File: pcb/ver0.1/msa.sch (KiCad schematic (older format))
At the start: 55 parts, among them J1 USB_A, J2 SWD Prog, U1 MCP1702, U2 MP23DB01HPTR, U3 W25Q128JV, U4 RP2040, U5 MP23DB01HPTR, U6 MP23DB01HPTR, U7 MP23DB01HPTR, Y1 H130B-12.000-20-3050-EXT-TR

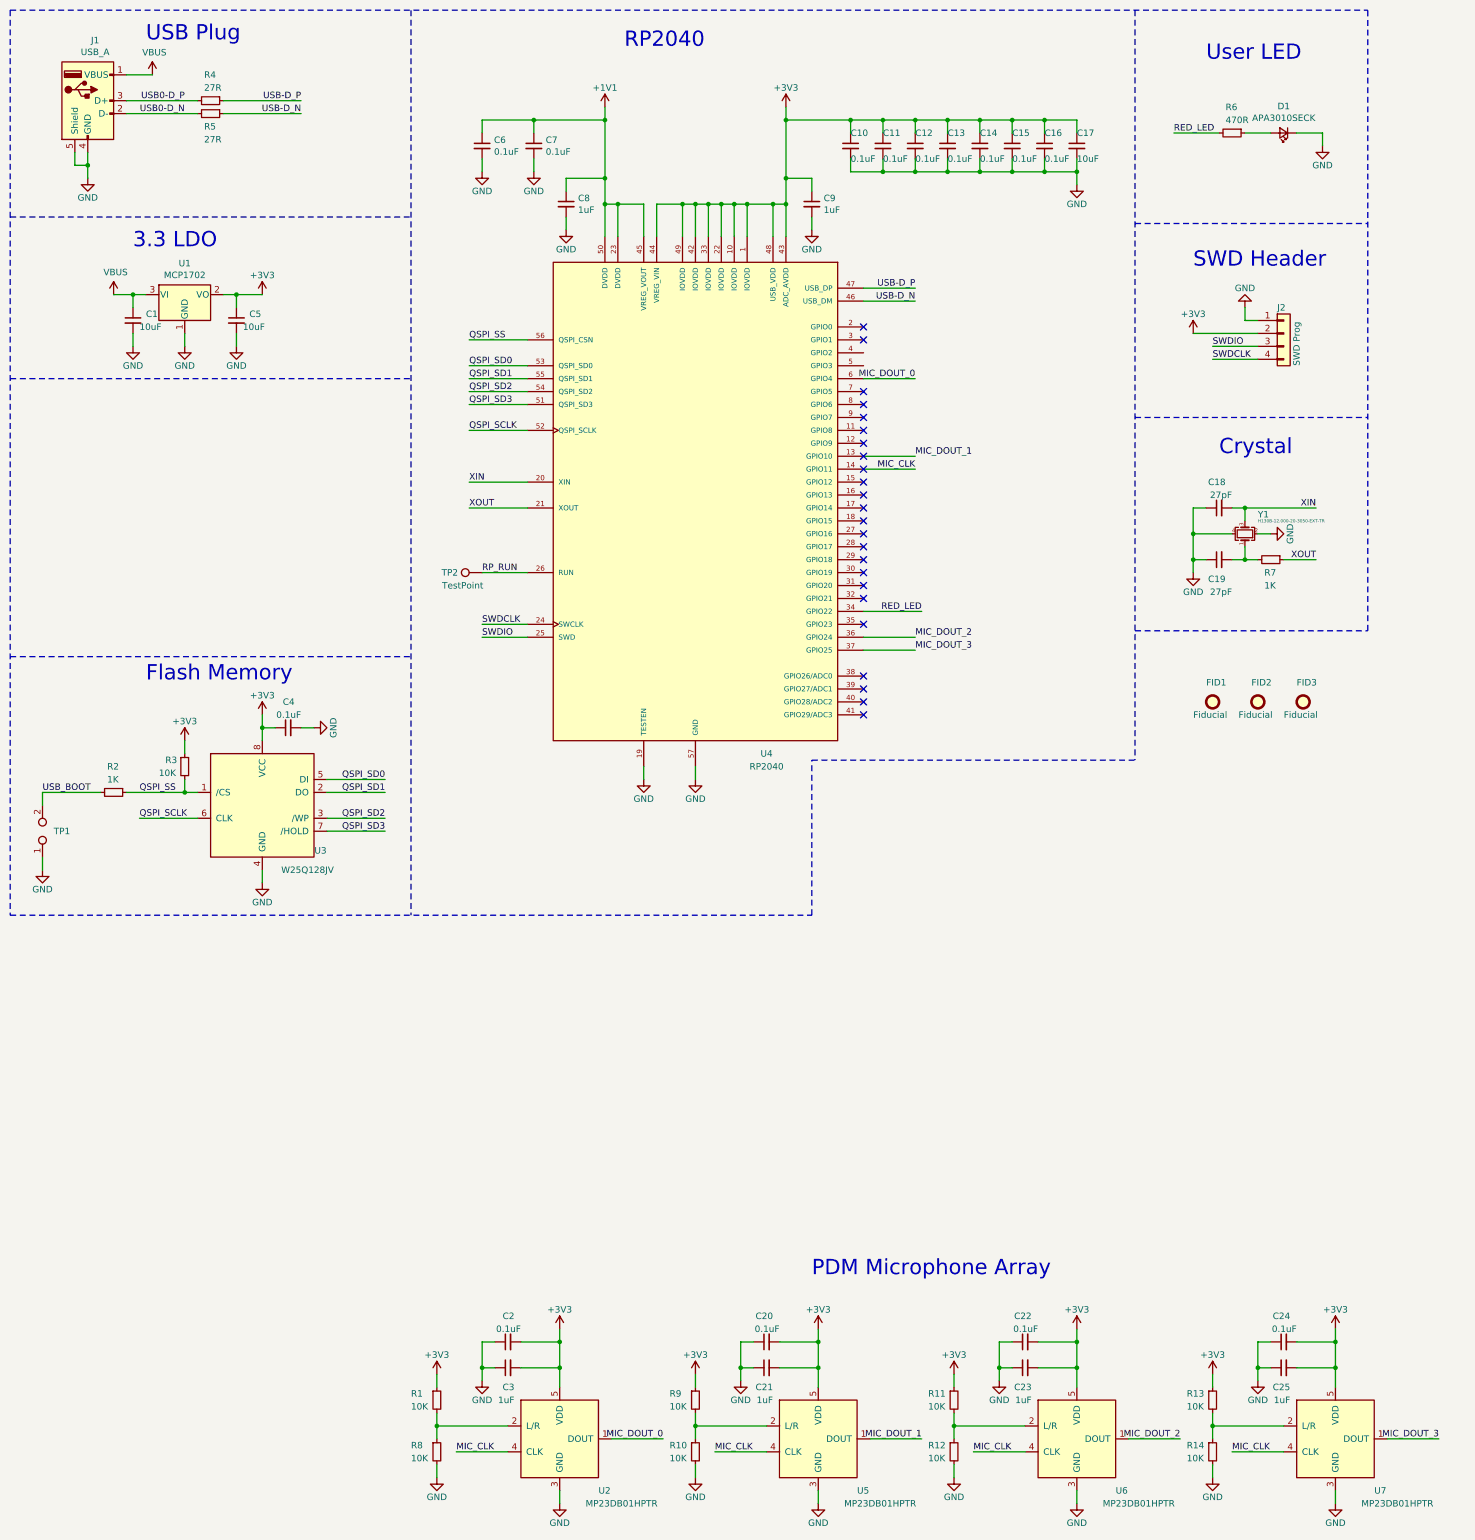
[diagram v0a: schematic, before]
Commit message: add test pads, last check before order PCB
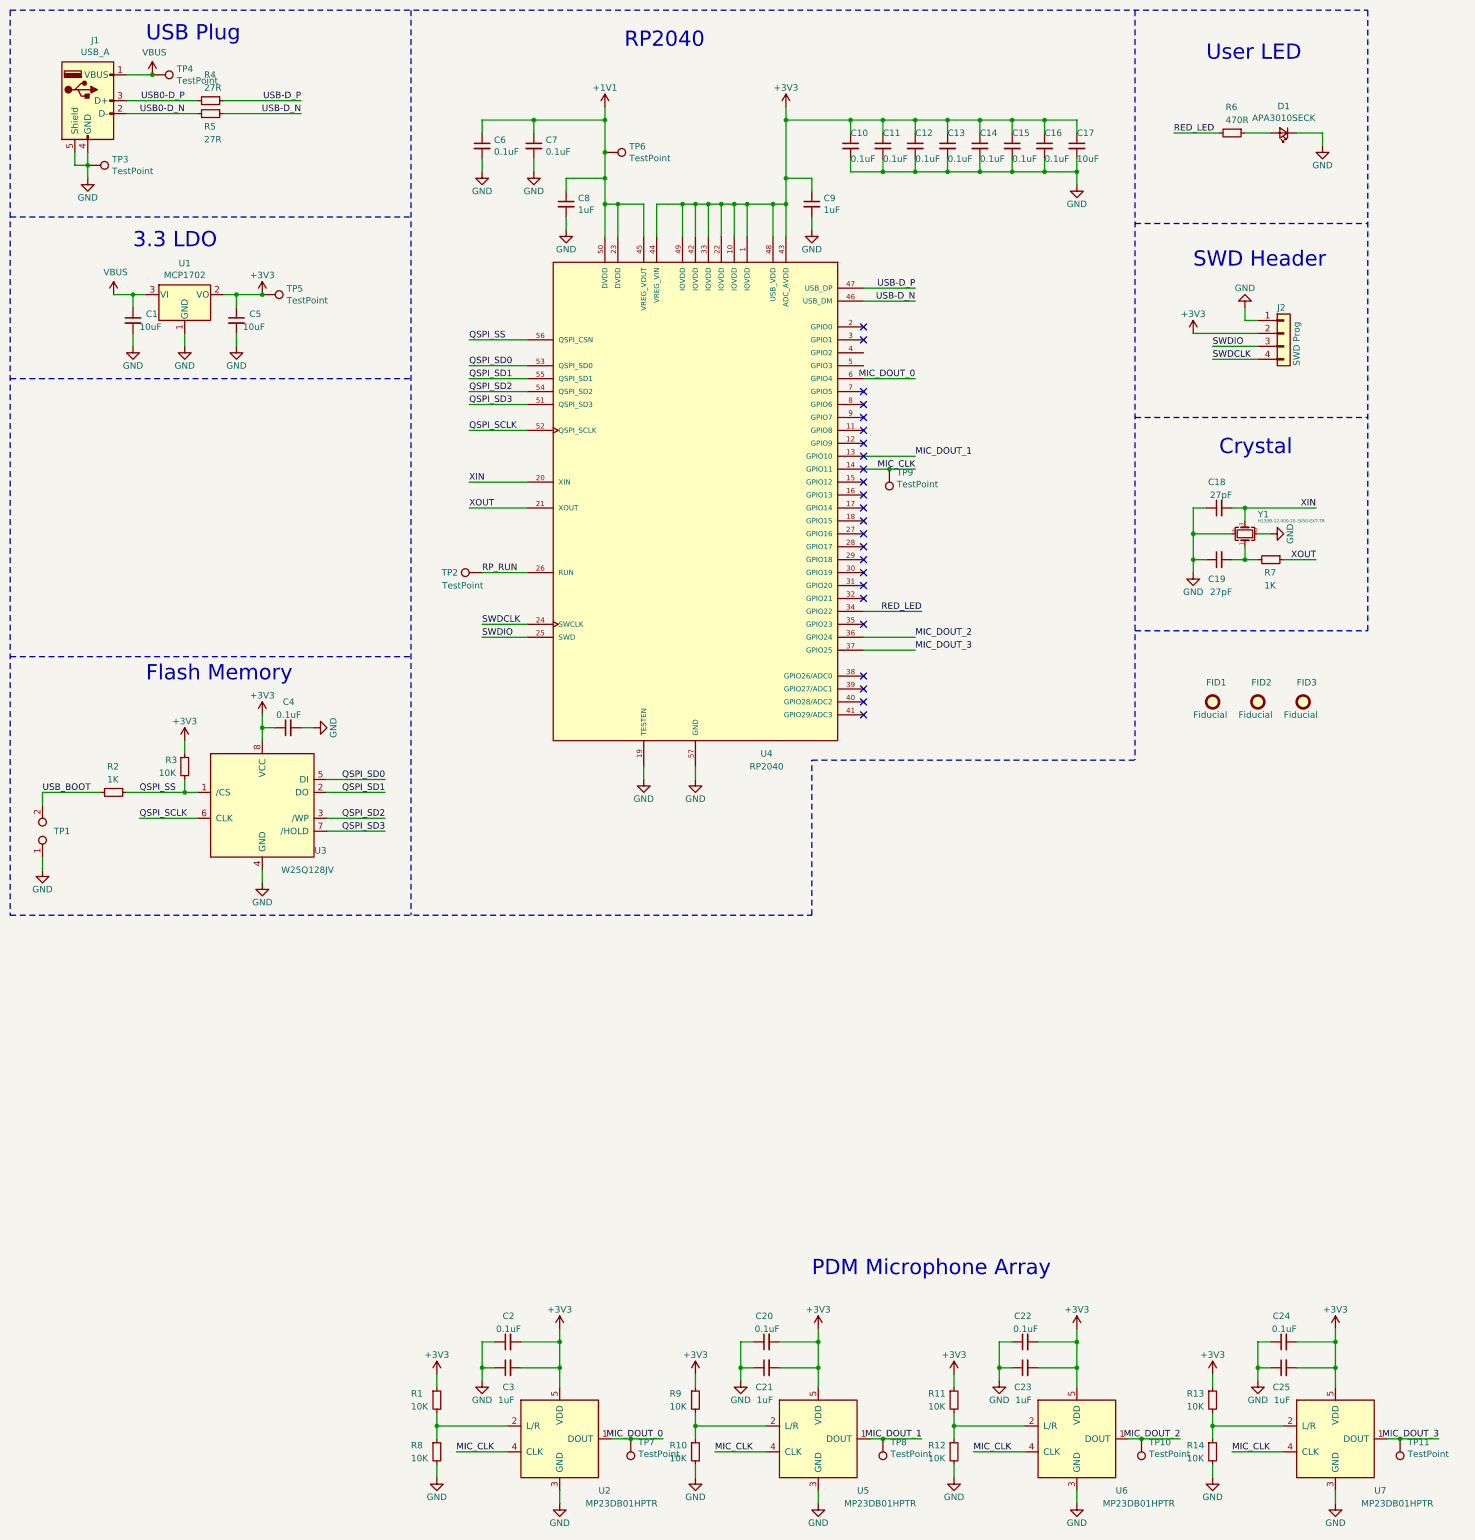
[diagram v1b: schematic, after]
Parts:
- added TP10, TP11, TP3, TP4, TP5, TP6, TP7, TP8, TP9: TestPoint, mico:SMD_1x01_P1.27mm, symbol Connector:TestPoint
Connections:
- net +1V1: now also TP6.1
- net +3V3: now also TP5.1
- net GND: now also TP3.1
- net MIC_CLK: now also TP9.1
- net MIC_DOUT_0: now also TP7.1
- net MIC_DOUT_1: now also TP8.1
- net MIC_DOUT_2: now also TP10.1
- net MIC_DOUT_3: now also TP11.1
- net VBUS: now also TP4.1
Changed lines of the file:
@@
 	4650 1450 4250 1450
 Wire Wire Line
-	5200 1450 5200 1900
+	5200 1450 5200 1700
 Wire Wire Line
 	4650 1450 5200 1450
@@
 	1100 1700 1100 1800
 Wire Wire Line
-	1100 1800 1200 1800
-Wire Wire Line
 	1200 1800 1200 1700
 Wire Wire Line
@@
 $EndComp
 Wire Wire Line
-	5250 11650 5650 11650
+	5250 11650 5400 11650
 Wire Wire Line
 	4450 11750 4050 11750
@@
 $EndComp
 Wire Wire Line
-	7250 11650 7650 11650
+	7250 11650 7350 11650
 Wire Wire Line
 	6450 11750 6050 11750
@@
 $EndComp
 Wire Wire Line
-	9250 11650 9650 11650
+	9250 11650 9350 11650
 Wire Wire Line
 	8450 11750 8050 11750
@@
 $EndComp
 Wire Wire Line
-	11250 11650 11650 11650
+	11250 11650 11350 11650
 Wire Wire Line
 	10450 11750 10050 11750
@@
 	7200 4050 7600 4050
 Wire Wire Line
-	7200 4150 7600 4150
+	7200 4150 7400 4150
 Wire Wire Line
 	7200 3450 7600 3450
@@
 Wire Wire Line
 	7650 5250 7200 5250
+$Comp
+L Connector:TestPoint TP7
+U 1 1 6206D2D0
+P 5400 11650
+F 0 "TP7" H 5342 11676 50  0000 R CNN
+F 1 "TestPoint" H 5342 11767 50  0000 R CNN
+F 2 "mico:SMD_1x01_P1.27mm" H 5600 11650 50  0001 C CNN
+F 3 "~" H 5600 11650 50  0001 C CNN
+	1    5400 11650
+	-1   0    0    1
+$EndComp
+Connection ~ 5400 11650
+Wire Wire Line
+	5400 11650 5650 11650
+$Comp
+L Connector:TestPoint TP8
+U 1 1 6206DDB3
+P 7350 11650
+F 0 "TP8" H 7292 11676 50  0000 R CNN
+F 1 "TestPoint" H 7292 11767 50  0000 R CNN
+F 2 "mico:SMD_1x01_P1.27mm" H 7550 11650 50  0001 C CNN
+F 3 "~" H 7550 11650 50  0001 C CNN
+	1    7350 11650
+	-1   0    0    1
+$EndComp
+Connection ~ 7350 11650
+Wire Wire Line
+	7350 11650 7650 11650
+$Comp
+L Connector:TestPoint TP10
+U 1 1 62073EE7
+P 9350 11650
+F 0 "TP10" H 9292 11676 50  0000 R CNN
+F 1 "TestPoint" H 9292 11767 50  0000 R CNN
+F 2 "mico:SMD_1x01_P1.27mm" H 9550 11650 50  0001 C CNN
+F 3 "~" H 9550 11650 50  0001 C CNN
+	1    9350 11650
+	-1   0    0    1
+$EndComp
+Connection ~ 9350 11650
+Wire Wire Line
+	9350 11650 9650 11650
+$Comp
+L Connector:TestPoint TP11
+U 1 1 620763A4
+P 11350 11650
+F 0 "TP11" H 11292 11676 50  0000 R CNN
+F 1 "TestPoint" H 11292 11767 50  0000 R CNN
+F 2 "mico:SMD_1x01_P1.27mm" H 11550 11650 50  0001 C CNN
+F 3 "~" H 11550 11650 50  0001 C CNN
+	1    11350 11650
+	-1   0    0    1
+$EndComp
+Connection ~ 11350 11650
+Wire Wire Line
+	11350 11650 11650 11650
+Wire Wire Line
+	1100 1800 1200 1800
+$Comp
+L Connector:TestPoint TP3
+U 1 1 6207B42E
+P 1200 1800
+F 0 "TP3" V 1154 1988 50  0000 L CNN
+F 1 "TestPoint" V 1245 1988 50  0000 L CNN
+F 2 "mico:SMD_1x01_P1.27mm" H 1400 1800 50  0001 C CNN
+F 3 "~" H 1400 1800 50  0001 C CNN
+	1    1200 1800
+	0    1    1    0
+$EndComp
+$Comp
+L Connector:TestPoint TP4
+U 1 1 62080B84
+P 1700 1100
+F 0 "TP4" V 1654 1288 50  0000 L CNN
+F 1 "TestPoint" V 1745 1288 50  0000 L CNN
+F 2 "mico:SMD_1x01_P1.27mm" H 1900 1100 50  0001 C CNN
+F 3 "~" H 1900 1100 50  0001 C CNN
+	1    1700 1100
+	0    1    1    0
+$EndComp
+Connection ~ 1700 1100
+$Comp
+L Connector:TestPoint TP5
+U 1 1 62082521
+P 2550 2800
+F 0 "TP5" V 2504 2988 50  0000 L CNN
+F 1 "TestPoint" V 2595 2988 50  0000 L CNN
+F 2 "mico:SMD_1x01_P1.27mm" H 2750 2800 50  0001 C CNN
+F 3 "~" H 2750 2800 50  0001 C CNN
+	1    2550 2800
+	0    1    1    0
+$EndComp
+Connection ~ 2550 2800
+$Comp
+L Connector:TestPoint TP6
+U 1 1 620829BE
+P 5200 1700
+F 0 "TP6" V 5154 1888 50  0000 L CNN
+F 1 "TestPoint" V 5245 1888 50  0000 L CNN
+F 2 "mico:SMD_1x01_P1.27mm" H 5400 1700 50  0001 C CNN
+F 3 "~" H 5400 1700 50  0001 C CNN
+	1    5200 1700
+	0    1    1    0
+$EndComp
+Connection ~ 5200 1700
+Wire Wire Line
+	5200 1700 5200 1900
+$Comp
+L Connector:TestPoint TP9
+U 1 1 62089103
+P 7400 4150
+F 0 "TP9" H 7342 4176 50  0000 R CNN
+F 1 "TestPoint" H 7342 4267 50  0000 R CNN
+F 2 "mico:SMD_1x01_P1.27mm" H 7600 4150 50  0001 C CNN
+F 3 "~" H 7600 4150 50  0001 C CNN
+	1    7400 4150
+	-1   0    0    1
+$EndComp
+Connection ~ 7400 4150
+Wire Wire Line
+	7400 4150 7600 4150
 $EndSCHEMATC
